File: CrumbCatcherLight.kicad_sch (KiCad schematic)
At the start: 10 parts, among them J1 USB_C_Receptacle_USB2.0, U2 ECMF02-2AMX6, U3 LP38691SDX-3.3

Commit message: Start component selection
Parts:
- removed C13: 10uF, Capacitor_SMD:C_0805_2012Metric, symbol Device:C_Small
- removed U3: LP38691SDX-3.3, Package_SON:WSON-6-1EP_3x3mm_P0.95mm, symbol Regulator_Linear:LP38691SD-3.3
- C1: renamed from C10; value 10nF -> 100nF; MPN C0402C103K3REC7411 -> C0402C104K3RAC7867; Price $0.16 -> $0.33; Rating CAP CER 0402 10NF 25V X7R 10% -> CAP CER 0.1UF 25V X7R 0402; Supplier PN 399-C0402C103K3REC7411CT-ND -> 399-14148-1-ND
- C2: renamed from C11; MPN C0402C104K3RAC7867 KEMET $0.33 CAP CER 0.1UF 25V X7R 0402 D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 -> C0402C104K3RAC7867
- C3: renamed from C12; value 10uF -> 10uF; footprint Capacitor_SMD:C_0805_2012Metric -> Capacitor_SMD:C_0402_1005Metric
- J1: MPN (none) -> USB4105; Manufacturer (none) -> GCT; Price (none) -> $1.29; Rating (none) -> CONN RCP USB2.0 TYP C 24P SMD RA; Supplier (none) -> Digikey; Supplier PN (none) -> 2073-USB4105-GF-ACT-ND
- U1: renamed from U2; MPN (none) -> ECMF02-2AMX6; Manufacturer (none) -> STMicroelectronics; Price (none) -> $0.83; Rating (none) -> CMC 200MA 2LN SMD ESD; Supplier (none) -> Digikey; Supplier PN (none) -> 497-10773-1-ND
- renumbered R2 to R1, R3 to R2
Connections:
- net +5V: now reaches C2.1, C3.1, FB1.2
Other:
- removed sheet STM32F0
- added sheet RP2040 (mad_lib/schematics/MCU/RP2040.kicad_sch)

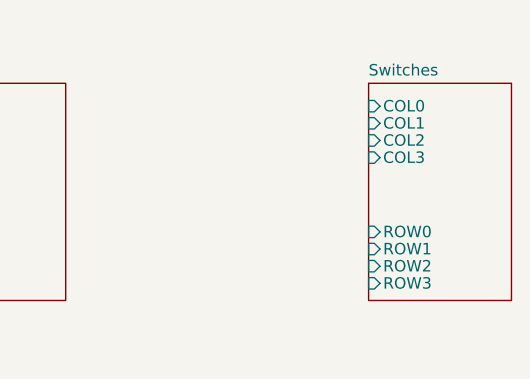
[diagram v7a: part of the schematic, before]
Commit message: Select last few components, add and cleanup footprints
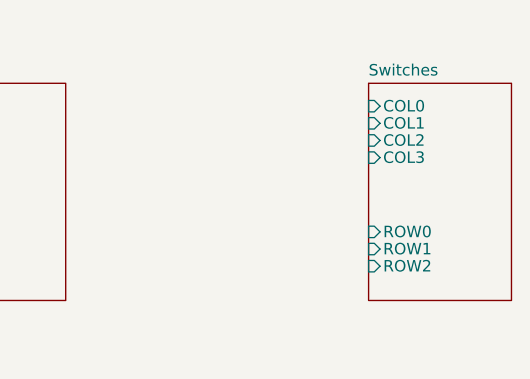
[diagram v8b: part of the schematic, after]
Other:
- sheet Switches ports: added none; removed ROW3
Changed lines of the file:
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@@
 		(dnp no)
 		(fields_autoplaced yes)
-		(property "Reference" "#PWR05"
+		(property "Reference" "#PWR07"
 			(at 130.81 27.94 0)
 			(effects
@@
 			(project "CrumbCatcherLight"
 				(path "/eedae293-eb5b-47bd-b383-bccfdf81bf72"
-					(reference "#PWR05")
+					(reference "#PWR07")
 					(unit 1)
 				)
@@
 		(dnp no)
 		(fields_autoplaced yes)
-		(property "Reference" "#PWR07"
+		(property "Reference" "#PWR05"
 			(at 107.95 99.06 0)
 			(effects
@@
 			(project "CrumbCatcherLight"
 				(path "/eedae293-eb5b-47bd-b383-bccfdf81bf72"
-					(reference "#PWR07")
+					(reference "#PWR05")
 					(unit 1)
 				)
@@
 		(on_board yes)
 		(dnp no)
-		(property "Reference" "#PWR08"
+		(property "Reference" "#PWR06"
 			(at 107.95 127 0)
 			(effects
@@
 			(project "CrumbCatcherLight"
 				(path "/eedae293-eb5b-47bd-b383-bccfdf81bf72"
-					(reference "#PWR08")
+					(reference "#PWR06")
 					(unit 1)
 				)
@@
 		(on_board yes)
 		(dnp no)
-		(property "Reference" "#PWR06"
+		(property "Reference" "#PWR08"
 			(at 130.81 49.53 0)
 			(effects
@@
 			(project "CrumbCatcherLight"
 				(path "/eedae293-eb5b-47bd-b383-bccfdf81bf72"
-					(reference "#PWR06")
+					(reference "#PWR08")
 					(unit 1)
 				)
@@
 			(effects
 				(font
-					(size 1.27 1.27)
-				)
-				(justify left)
-			)
-		)
-		(pin "ROW3" input
-			(at 189.865 117.475 180)
-			(effects
-				(font
